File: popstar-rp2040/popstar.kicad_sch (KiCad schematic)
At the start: 31 parts, among them J1 JST SH 4-pin, J2 SWD, SW1 Boot, U2 XC6206PxxxMR, U3 SRV05-4, U4 W25Q128JVS, U6 RP2040, Y1 12MHz

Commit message: Finished placing all components within the courtyard.
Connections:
- net +5V: now also U3.5 (VP)
- net GND: now also J2.1 (Pin_1); no longer J2.3 (Pin_3)
- net VBUS: no longer U3.5 (VP)
- net ~{RESET}: now also J2.3 (Pin_3); no longer J2.1 (Pin_1)
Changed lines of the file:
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@@
+    (stroke (width 0) (type default))
+  )
+  (wire (pts (xy 262.89 83.82) (xy 272.415 83.82))
     (stroke (width 0) (type default))
   )
@@
     (stroke (width 0) (type default))
   )
-  (wire (pts (xy 262.89 86.36) (xy 275.59 86.36))
+  (wire (pts (xy 262.89 81.28) (xy 281.305 81.28))
     (stroke (width 0) (type default))
   )
@@
     (stroke (width 0) (type default))
   )
-  (wire (pts (xy 262.89 83.82) (xy 275.59 83.82))
-    (stroke (width 0) (type default))
-  )
   (wire (pts (xy 22.86 54.61) (xy 29.21 54.61))
     (stroke (width 0) (type default))
@@
     (stroke (width 0) (type default))
   )
+  (wire (pts (xy 272.415 83.82) (xy 272.415 86.36))
+    (stroke (width 0) (type default))
+  )
   (wire (pts (xy 181.61 120.65) (xy 173.99 120.65))
     (stroke (width 0) (type default))
@@
   )
   (wire (pts (xy 204.47 121.92) (xy 204.47 120.65))
+    (stroke (width 0) (type default))
+  )
+  (wire (pts (xy 272.415 86.36) (xy 276.225 86.36))
     (stroke (width 0) (type default))
   )
@@
     )
   )
-  (global_label "~{RESET}" (shape input) (at 262.89 81.28 0) (fields_autoplaced)
-    (effects (font (size 1.27 1.27)) (justify left))
-    (property "Intersheetrefs" "${INTERSHEET_REFS}" (at 271.5409 81.28 0)
+  (global_label "~{RESET}" (shape input) (at 262.89 86.36 0) (fields_autoplaced)
+    (effects (font (size 1.27 1.27)) (justify left))
+    (property "Intersheetrefs" "${INTERSHEET_REFS}" (at 271.5409 86.36 0)
       (effects (font (size 1.27 1.27)) (justify left) hide)
     )
@@
     )
   )
-  (symbol (lib_id "power:GND") (at 275.59 86.36 0) (unit 1)
-    (in_bom yes) (on_board yes) (dnp no) (fields_autoplaced)
-    (property "Reference" "#PWR017" (at 275.59 92.71 0)
-      (effects (font (size 1.27 1.27)) hide)
-    )
-    (property "Value" "GND" (at 275.59 91.44 0)
-      (effects (font (size 1.27 1.27)))
-    )
-    (property "Footprint" "" (at 275.59 86.36 0)
-      (effects (font (size 1.27 1.27)) hide)
-    )
-    (property "Datasheet" "" (at 275.59 86.36 0)
+  (symbol (lib_id "power:GND") (at 281.305 81.28 0) (unit 1)
+    (in_bom yes) (on_board yes) (dnp no)
+    (property "Reference" "#PWR017" (at 281.305 87.63 0)
+      (effects (font (size 1.27 1.27)) hide)
+    )
+    (property "Value" "GND" (at 281.305 85.09 0)
+      (effects (font (size 1.27 1.27)))
+    )
+    (property "Footprint" "" (at 281.305 81.28 0)
+      (effects (font (size 1.27 1.27)) hide)
+    )
+    (property "Datasheet" "" (at 281.305 81.28 0)
       (effects (font (size 1.27 1.27)) hide)
     )
@@
     )
   )
+  (symbol (lib_id "power:+5V") (at 261.62 22.86 0) (unit 1)
+    (in_bom yes) (on_board yes) (dnp no)
+    (property "Reference" "#PWR037" (at 261.62 26.67 0)
+      (effects (font (size 1.27 1.27)) hide)
+    )
+    (property "Value" "+5V" (at 261.62 19.05 0)
+      (effects (font (size 1.27 1.27)))
+    )
+    (property "Footprint" "" (at 261.62 22.86 0)
+      (effects (font (size 1.27 1.27)) hide)
+    )
+    (property "Datasheet" "" (at 261.62 22.86 0)
+      (effects (font (size 1.27 1.27)) hide)
+    )
+    (pin "1")
+    (instances
+      (project "popstar"
+        (path "/2b78fc64-feb6-4bfa-a478-e5c73a3e42a2"
+          (reference "#PWR037") (unit 1)
+        )
+      )
+    )
+  )
   (symbol (lib_id "power:+3V3") (at 165.735 24.765 0) (unit 1)
     (in_bom yes) (on_board yes) (dnp no) (fields_autoplaced)
@@
     )
   )
-  (symbol (lib_id "power:+3V3") (at 275.59 83.82 0) (unit 1)
-    (in_bom yes) (on_board yes) (dnp no) (fields_autoplaced)
-    (property "Reference" "#PWR018" (at 275.59 87.63 0)
-      (effects (font (size 1.27 1.27)) hide)
-    )
-    (property "Value" "+3V3" (at 275.59 80.01 0)
-      (effects (font (size 1.27 1.27)))
-    )
-    (property "Footprint" "" (at 275.59 83.82 0)
-      (effects (font (size 1.27 1.27)) hide)
-    )
-    (property "Datasheet" "" (at 275.59 83.82 0)
+  (symbol (lib_id "power:+3V3") (at 276.225 86.36 0) (unit 1)
+    (in_bom yes) (on_board yes) (dnp no)
+    (property "Reference" "#PWR018" (at 276.225 90.17 0)
+      (effects (font (size 1.27 1.27)) hide)
+    )
+    (property "Value" "+3V3" (at 275.59 82.55 0)
+      (effects (font (size 1.27 1.27)))
+    )
+    (property "Footprint" "" (at 276.225 86.36 0)
+      (effects (font (size 1.27 1.27)) hide)
+    )
+    (property "Datasheet" "" (at 276.225 86.36 0)
       (effects (font (size 1.27 1.27)) hide)
     )
@@
         )
       )
-    )
-  )
-  (symbol (lib_id "power:VBUS") (at 261.62 22.86 0) (unit 1)
-    (in_bom yes) (on_board yes) (dnp no) (fields_autoplaced)
-    (property "Reference" "#PWR022" (at 261.62 26.67 0)
-      (effects (font (size 1.27 1.27)) hide)
-    )
-    (property "Value" "VBUS" (at 261.62 19.05 0)
-      (effects (font (size 1.27 1.27)))
-    )
-    (property "Footprint" "" (at 261.62 22.86 0)
-      (effects (font (size 1.27 1.27)) hide)
-    )
-    (property "Datasheet" "" (at 261.62 22.86 0)
-      (effects (font (size 1.27 1.27)) hide)
-    )
-    (pin "1")
-    (instances
-      (project "popstar"
-        (path "/2b78fc64-feb6-4bfa-a478-e5c73a3e42a2"
-          (reference "#PWR022") (unit 1)
-        )
-      )

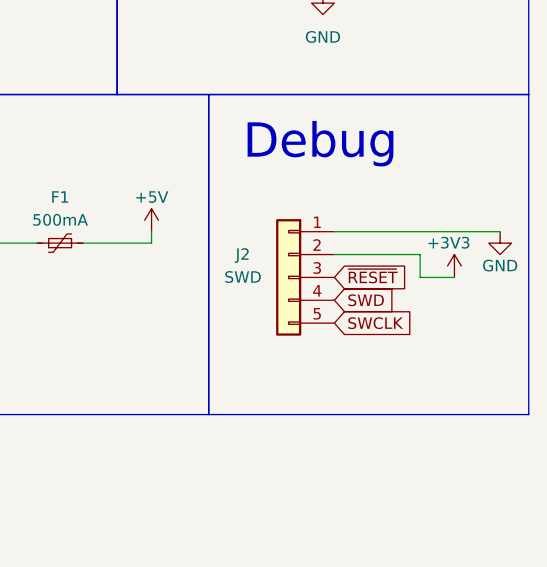
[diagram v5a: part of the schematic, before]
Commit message: Routed debug
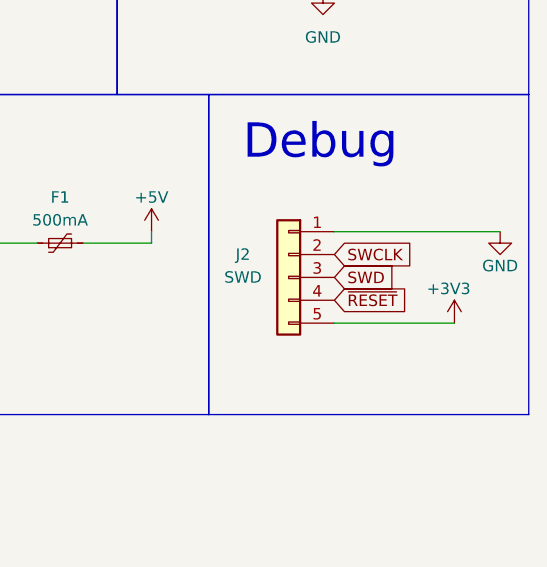
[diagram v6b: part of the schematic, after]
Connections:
- net +3V3: now also J2.5 (Pin_5); no longer J2.2 (Pin_2)
- net SWCLK: now also J2.2 (Pin_2); no longer J2.5 (Pin_5)
- net SWD: now also J2.3 (Pin_3); no longer J2.4 (Pin_4)
- net ~{RESET}: now also J2.4 (Pin_4); no longer J2.3 (Pin_3)
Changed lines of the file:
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@@
-    (stroke (width 0) (type default))
-  )
-  (wire (pts (xy 262.89 83.82) (xy 272.415 83.82))
     (stroke (width 0) (type default))
   )
@@
     (stroke (width 0) (type default))
   )
-  (wire (pts (xy 272.415 83.82) (xy 272.415 86.36))
-    (stroke (width 0) (type default))
-  )
   (wire (pts (xy 181.61 120.65) (xy 173.99 120.65))
     (stroke (width 0) (type default))
@@
     (stroke (width 0) (type default))
   )
+  (wire (pts (xy 262.89 91.44) (xy 276.225 91.44))
+    (stroke (width 0) (type default))
+  )
   (wire (pts (xy 166.37 127) (xy 166.37 128.27))
     (stroke (width 0) (type default))
   )
   (wire (pts (xy 204.47 121.92) (xy 204.47 120.65))
-    (stroke (width 0) (type default))
-  )
-  (wire (pts (xy 272.415 86.36) (xy 276.225 86.36))
     (stroke (width 0) (type default))
   )
@@
     )
   )
-  (global_label "SWD" (shape input) (at 262.89 88.9 0) (fields_autoplaced)
-    (effects (font (size 1.27 1.27)) (justify left))
-    (property "Intersheetrefs" "${INTERSHEET_REFS}" (at 269.7267 88.9 0)
+  (global_label "SWD" (shape input) (at 262.89 86.36 0) (fields_autoplaced)
+    (effects (font (size 1.27 1.27)) (justify left))
+    (property "Intersheetrefs" "${INTERSHEET_REFS}" (at 269.7267 86.36 0)
       (effects (font (size 1.27 1.27)) (justify left) hide)
     )
@@
     )
   )
-  (global_label "~{RESET}" (shape input) (at 262.89 86.36 0) (fields_autoplaced)
-    (effects (font (size 1.27 1.27)) (justify left))
-    (property "Intersheetrefs" "${INTERSHEET_REFS}" (at 271.5409 86.36 0)
+  (global_label "~{RESET}" (shape input) (at 262.89 88.9 0) (fields_autoplaced)
+    (effects (font (size 1.27 1.27)) (justify left))
+    (property "Intersheetrefs" "${INTERSHEET_REFS}" (at 271.5409 88.9 0)
       (effects (font (size 1.27 1.27)) (justify left) hide)
     )
@@
     )
   )
-  (global_label "SWCLK" (shape input) (at 262.89 91.44 0) (fields_autoplaced)
-    (effects (font (size 1.27 1.27)) (justify left))
-    (property "Intersheetrefs" "${INTERSHEET_REFS}" (at 272.0248 91.44 0)
+  (global_label "SWCLK" (shape input) (at 262.89 83.82 0) (fields_autoplaced)
+    (effects (font (size 1.27 1.27)) (justify left))
+    (property "Intersheetrefs" "${INTERSHEET_REFS}" (at 272.0248 83.82 0)
       (effects (font (size 1.27 1.27)) (justify left) hide)
     )
@@
     )
   )
-  (symbol (lib_id "power:+3V3") (at 276.225 86.36 0) (unit 1)
-    (in_bom yes) (on_board yes) (dnp no)
-    (property "Reference" "#PWR018" (at 276.225 90.17 0)
-      (effects (font (size 1.27 1.27)) hide)
-    )
-    (property "Value" "+3V3" (at 275.59 82.55 0)
-      (effects (font (size 1.27 1.27)))
-    )
-    (property "Footprint" "" (at 276.225 86.36 0)
-      (effects (font (size 1.27 1.27)) hide)
-    )
-    (property "Datasheet" "" (at 276.225 86.36 0)
-      (effects (font (size 1.27 1.27)) hide)
-    )
+  (symbol (lib_id "power:+3V3") (at 276.225 91.44 0) (unit 1)
+    (in_bom yes) (on_board yes) (dnp no)
+    (property "Reference" "#PWR018" (at 276.225 95.25 0)
+      (effects (font (size 1.27 1.27)) hide)
+    )
+    (property "Value" "+3V3" (at 275.59 87.63 0)
+      (effects (font (size 1.27 1.27)))
+    )
+    (property "Footprint" "" (at 276.225 91.44 0)
+      (effects (font (size 1.27 1.27)) hide)
+    )
+    (property "Datasheet" "" (at 276.225 91.44 0)
+      (effects (font (size 1.27 1.27)) hide)
+    )

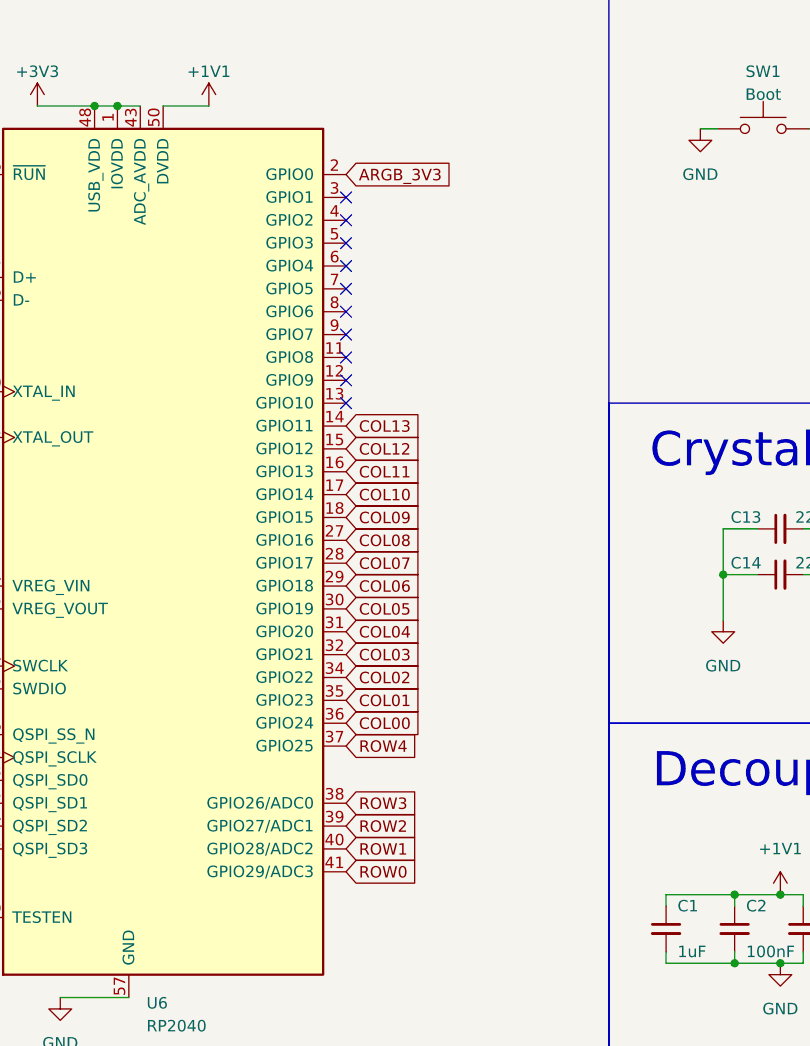
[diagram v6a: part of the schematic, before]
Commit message: Routed crystal oscillator, changed up GPIO pins for cleaner switch matrix routing
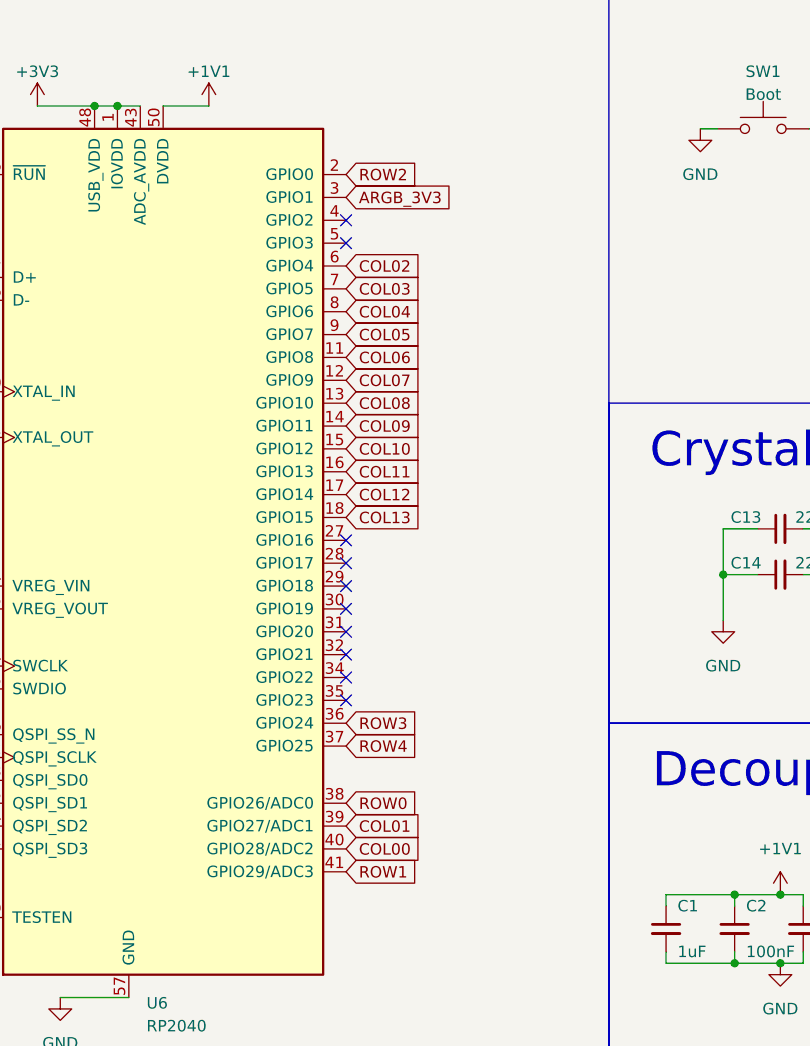
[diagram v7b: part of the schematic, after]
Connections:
- net ARGB_3V3: now also U6.3 (GPIO1); no longer U6.2 (GPIO0)
- net COL00: now also U6.40 (GPIO28/ADC2); no longer U6.36 (GPIO24)
- net COL01: now also U6.39 (GPIO27/ADC1); no longer U6.35 (GPIO23)
- net COL02: now also U6.6 (GPIO4); no longer U6.34 (GPIO22)
- net COL03: now also U6.7 (GPIO5); no longer U6.32 (GPIO21)
- net COL04: now also U6.8 (GPIO6); no longer U6.31 (GPIO20)
- net COL05: now also U6.9 (GPIO7); no longer U6.30 (GPIO19)
- net COL06: now also U6.11 (GPIO8); no longer U6.29 (GPIO18)
- net COL07: now also U6.12 (GPIO9); no longer U6.28 (GPIO17)
- net COL08: now also U6.13 (GPIO10); no longer U6.27 (GPIO16)
- net COL09: now also U6.14 (GPIO11); no longer U6.18 (GPIO15)
- net COL10: now also U6.15 (GPIO12); no longer U6.17 (GPIO14)
- net COL12: now also U6.17 (GPIO14); no longer U6.15 (GPIO12)
- net COL13: now also U6.18 (GPIO15); no longer U6.14 (GPIO11)
- net ROW0: now also U6.38 (GPIO26/ADC0); no longer U6.41 (GPIO29/ADC3)
- net ROW1: now also U6.41 (GPIO29/ADC3); no longer U6.40 (GPIO28/ADC2)
- net ROW2: now also U6.2 (GPIO0); no longer U6.39 (GPIO27/ADC1)
- net ROW3: now also U6.36 (GPIO24); no longer U6.38 (GPIO26/ADC0)

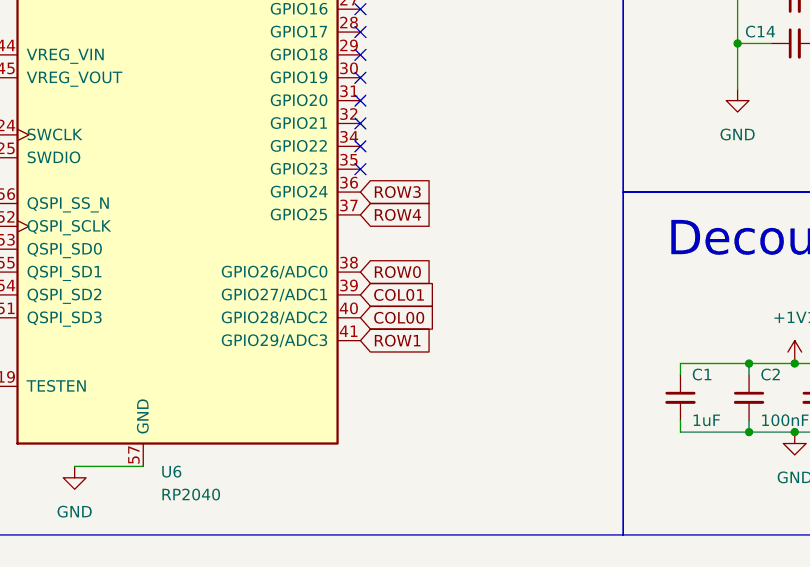
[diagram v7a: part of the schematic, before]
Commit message: Finished routing rows, cleaned up existing traces. Switched row0 and col0 for cleaner routing.
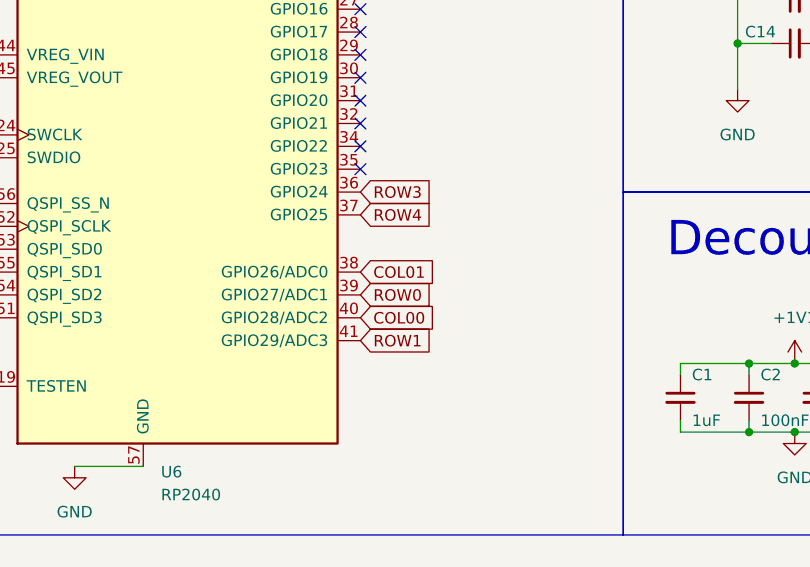
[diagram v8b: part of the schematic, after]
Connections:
- net COL01: now also U6.38 (GPIO26/ADC0); no longer U6.39 (GPIO27/ADC1)
- net ROW0: now also U6.39 (GPIO27/ADC1); no longer U6.38 (GPIO26/ADC0)
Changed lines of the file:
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@@
     )
   )
-  (global_label "ROW0" (shape input) (at 85.09 110.49 0) (fields_autoplaced)
+  (global_label "ROW0" (shape input) (at 85.09 113.03 0) (fields_autoplaced)
     (effects (font (size 1.27 1.27)) (justify left))
-    (property "Intersheetrefs" "${INTERSHEET_REFS}" (at 93.2572 110.49 0)
+    (property "Intersheetrefs" "${INTERSHEET_REFS}" (at 93.2572 113.03 0)
       (effects (font (size 1.27 1.27)) (justify left) hide)
     )
@@
     )
   )
-  (global_label "COL01" (shape input) (at 85.09 113.03 0) (fields_autoplaced)
+  (global_label "COL01" (shape input) (at 85.09 110.49 0) (fields_autoplaced)
     (effects (font (size 1.27 1.27)) (justify left))
-    (property "Intersheetrefs" "${INTERSHEET_REFS}" (at 94.0434 113.03 0)
+    (property "Intersheetrefs" "${INTERSHEET_REFS}" (at 94.0434 110.49 0)
       (effects (font (size 1.27 1.27)) (justify left) hide)
     )
